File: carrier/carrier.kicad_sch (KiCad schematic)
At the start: 10 parts

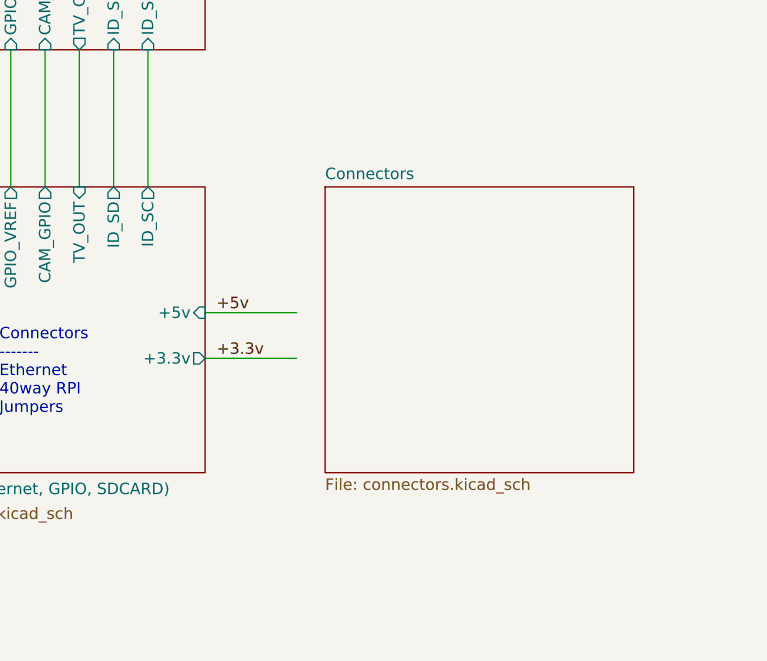
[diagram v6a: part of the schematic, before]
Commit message: Feat: begun work on finalizing PCB layout
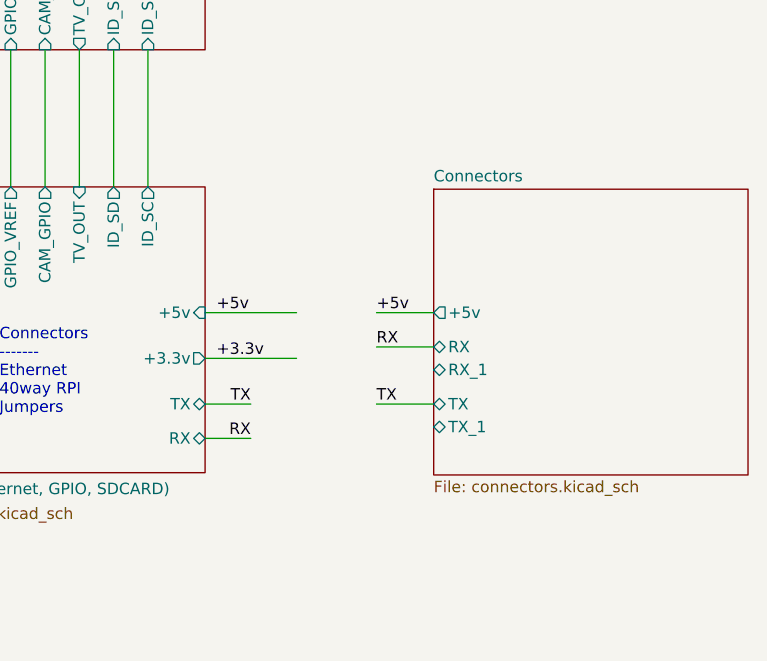
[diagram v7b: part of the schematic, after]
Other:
- sheet CM4_GPIO ( Ethernet, GPIO, SDCARD) ports: added RX, TX; removed none
- sheet Connectors ports: added +5v, RX, RX_1, TX, TX_1; removed none
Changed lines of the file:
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@@
+    (stroke (width 0) (type default))
+  )
+  (wire (pts (xy 138.43 143.51) (xy 143.51 143.51))
     (stroke (width 0) (type default))
   )
@@
     (stroke (width 0) (type solid))
   )
+  (wire (pts (xy 138.43 139.7) (xy 143.51 139.7))
+    (stroke (width 0) (type default))
+  )
   (wire (pts (xy 128.27 100.33) (xy 128.27 115.57))
     (stroke (width 0) (type solid))
   )
+  (wire (pts (xy 157.48 129.54) (xy 163.83 129.54))
+    (stroke (width 0) (type default))
+  )
   (wire (pts (xy 148.59 129.54) (xy 138.43 129.54))
     (stroke (width 0) (type solid))
@@
     (stroke (width 0) (type solid))
   )
+  (wire (pts (xy 157.48 133.35) (xy 163.83 133.35))
+    (stroke (width 0) (type default))
+  )
   (wire (pts (xy 31.75 106.68) (xy 39.37 106.68))
     (stroke (width 0) (type default))
@@
   (wire (pts (xy 110.49 106.045) (xy 110.49 115.57))
     (stroke (width 0) (type solid))
+  )
+  (wire (pts (xy 157.48 139.7) (xy 163.83 139.7))
+    (stroke (width 0) (type default))
   )
   (wire (pts (xy 101.6 80.01) (xy 88.9 80.01))
@@
     (effects (font (size 1.27 1.27)) (justify left bottom))
   )
+  (label "TX" (at 143.51 139.7 180) (fields_autoplaced)
+    (effects (font (size 1.27 1.27)) (justify right bottom))
+  )
   (label "+3.3v" (at 92.71 80.01 0) (fields_autoplaced)
     (effects (font (size 1.27 1.27)) (justify left bottom))
   )
+  (label "TX" (at 157.48 139.7 0) (fields_autoplaced)
+    (effects (font (size 1.27 1.27)) (justify left bottom))
+  )
   (label "nEXTRST" (at 76.2 64.77 0) (fields_autoplaced)
     (effects (font (size 1.27 1.27)) (justify left bottom))
@@
     (effects (font (size 1.27 1.27)) (justify left bottom))
   )
+  (label "+5v" (at 157.48 129.54 0) (fields_autoplaced)
+    (effects (font (size 1.27 1.27)) (justify left bottom))
+  )
   (label "GLOBAL_EN" (at 88.9 129.54 0) (fields_autoplaced)
+    (effects (font (size 1.27 1.27)) (justify left bottom))
+  )
+  (label "RX" (at 143.51 143.51 180) (fields_autoplaced)
+    (effects (font (size 1.27 1.27)) (justify right bottom))
+  )
+  (label "RX" (at 157.48 133.35 0) (fields_autoplaced)
     (effects (font (size 1.27 1.27)) (justify left bottom))
   )
@@
       (effects (font (size 1.27 1.27)) (justify right))
     )
+    (pin "TX" bidirectional (at 138.43 139.7 0)
+      (effects (font (size 1.27 1.27)) (justify right))
+    )
+    (pin "RX" bidirectional (at 138.43 143.51 0)
+      (effects (font (size 1.27 1.27)) (justify right))
+    )
     (instances
       (project "CM4IOv5"
@@
     )
   )
-  (sheet (at 151.765 115.57) (size 34.29 31.75) (fields_autoplaced)
+  (sheet (at 163.83 115.824) (size 34.925 31.75) (fields_autoplaced)
     (stroke (width 0.1524) (type solid))
     (fill (color 0 0 0 0.0000))
-    (property "Sheetname" "Connectors" (at 151.765 114.8584 0)
+    (property "Sheetname" "Connectors" (at 163.83 115.1124 0)
       (effects (font (size 1.27 1.27)) (justify left bottom))
     )
-    (property "Sheetfile" "connectors.kicad_sch" (at 151.765 147.9046 0)
+    (property "Sheetfile" "connectors.kicad_sch" (at 163.83 148.1586 0)
       (effects (font (size 1.27 1.27)) (justify left top))
     )
-    (instances
+    (pin "+5v" output (at 163.83 129.54 180)
+      (effects (font (size 1.27 1.27)) (justify left))
+    )
+    (pin "RX" bidirectional (at 163.83 133.35 180)
+      (effects (font (size 1.27 1.27)) (justify left))
+    )
+    (pin "RX_1" bidirectional (at 163.83 135.89 180)
+      (effects (font (size 1.27 1.27)) (justify left))
+    )
+    (pin "TX" bidirectional (at 163.83 139.7 180)
+      (effects (font (size 1.27 1.27)) (justify left))
+    )
+    (pin "TX_1" bidirectional (at 163.83 142.24 180)
+      (effects (font (size 1.27 1.27)) (justify left))
+    )
+    (instances

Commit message: Feat: first draft pcb layout
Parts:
- removed H7, H8: MountingHole, MountingHole:MountingHole_2.7mm_M2.5, symbol Mechanical:MountingHole
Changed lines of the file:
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@@
-    )
-  )
-  (symbol (lib_id "Mechanical:MountingHole") (at 43.815 182.245 0) (unit 1)
-    (in_bom yes) (on_board yes) (dnp no)
-    (property "Reference" "H8" (at 46.355 181.102 0)
-      (effects (font (size 1.27 1.27)) (justify left))
-    )
-    (property "Value" "MountingHole" (at 46.355 183.388 0)
-      (effects (font (size 1.27 1.27)) (justify left))
-    )
-    (property "Footprint" "MountingHole:MountingHole_2.7mm_M2.5" (at 43.815 182.245 0)
-      (effects (font (size 1.27 1.27)) hide)
-    )
-    (property "Datasheet" "~" (at 43.815 182.245 0)
-      (effects (font (size 1.27 1.27)) hide)
-    )
-    (property "Field4" "nf" (at 43.815 182.245 0)
-      (effects (font (size 1.27 1.27)) hide)
-    )
-    (property "Field5" "nf" (at 43.815 182.245 0)
-      (effects (font (size 1.27 1.27)) hide)
-    )
-    (property "Field6" "nf" (at 43.815 182.245 0)
-      (effects (font (size 1.27 1.27)) hide)
-    )
-    (property "Field7" "nf" (at 43.815 182.245 0)
-      (effects (font (size 1.27 1.27)) hide)
-    )
-    (property "Part Description" "M2.5 mounting hole" (at 43.815 182.245 0)
-      (effects (font (size 1.27 1.27)) hide)
-    )
-    (instances
-      (project "carrier"
-        (path "/4b1cea9d-93bc-4380-88c3-ede99bb53de2"
-          (reference "H8") (unit 1)
-        )
-      )
-      (project "CM4IOv5"
-        (path "/e63e39d7-6ac0-4ffd-8aa3-1841a4541b55"
-          (reference "H8") (unit 1)
-        )
-      )
     )
   )
@@
         )
       )
-    )
-  )
-  (symbol (lib_id "Mechanical:MountingHole") (at 43.815 177.165 0) (unit 1)
-    (in_bom yes) (on_board yes) (dnp no)
-    (property "Reference" "H7" (at 46.355 176.022 0)
-      (effects (font (size 1.27 1.27)) (justify left))
-    )
-    (property "Value" "MountingHole" (at 46.355 178.308 0)
-      (effects (font (size 1.27 1.27)) (justify left))
-    )
-    (property "Footprint" "MountingHole:MountingHole_2.7mm_M2.5" (at 43.815 177.165 0)
-      (effects (font (size 1.27 1.27)) hide)
-    )
-    (property "Datasheet" "~" (at 43.815 177.165 0)
-      (effects (font (size 1.27 1.27)) hide)
-    )
-    (property "Field4" "nf" (at 43.815 177.165 0)
-      (effects (font (size 1.27 1.27)) hide)
-    )
-    (property "Field5" "nf" (at 43.815 177.165 0)
-      (effects (font (size 1.27 1.27)) hide)
-    )
-    (property "Field6" "nf" (at 43.815 177.165 0)
-      (effects (font (size 1.27 1.27)) hide)
-    )
-    (property "Field7" "nf" (at 43.815 177.165 0)
-      (effects (font (size 1.27 1.27)) hide)
-    )
-    (property "Part Description" "M2.5 mounting hole" (at 43.815 177.165 0)
-      (effects (font (size 1.27 1.27)) hide)
-    )
-    (instances
-      (project "carrier"
-        (path "/4b1cea9d-93bc-4380-88c3-ede99bb53de2"
-          (reference "H7") (unit 1)
-        )
-      )
-      (project "CM4IOv5"
-        (path "/e63e39d7-6ac0-4ffd-8aa3-1841a4541b55"
-          (reference "H7") (unit 1)
-        )
-      )
